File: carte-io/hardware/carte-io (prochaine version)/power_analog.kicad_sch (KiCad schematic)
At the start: 38 parts, among them J1 USB_C_Receptacle_USB2.0_14P, J2 JST-XH_S2B-XH-A, J26 JST-PH-B2B, Q1 IRF9388TRPBF, U16 LT1963AxST-3.3, U2 FT231XQ, U3 LT1963AxST-3.3

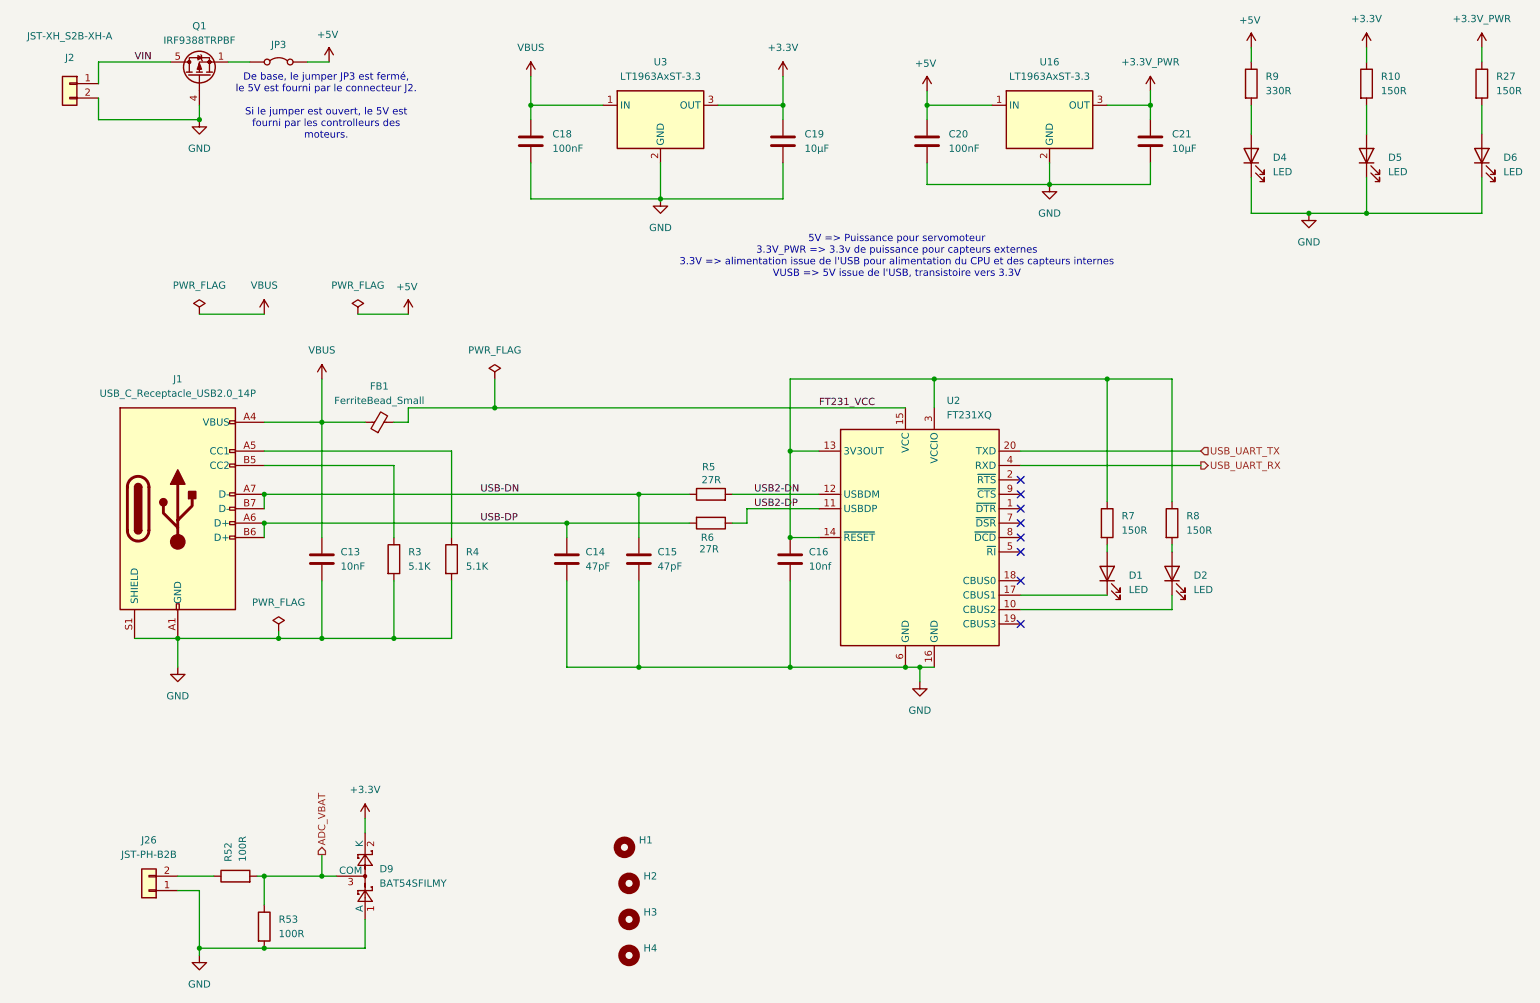
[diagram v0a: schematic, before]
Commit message: Commit de sauvegarde, gros changement sur la carte IO, les connecteurs sont compatibles SeeedStudio Grove. Il faut reprendre une grosse partie du routage et rajouter deux entrées analogiques
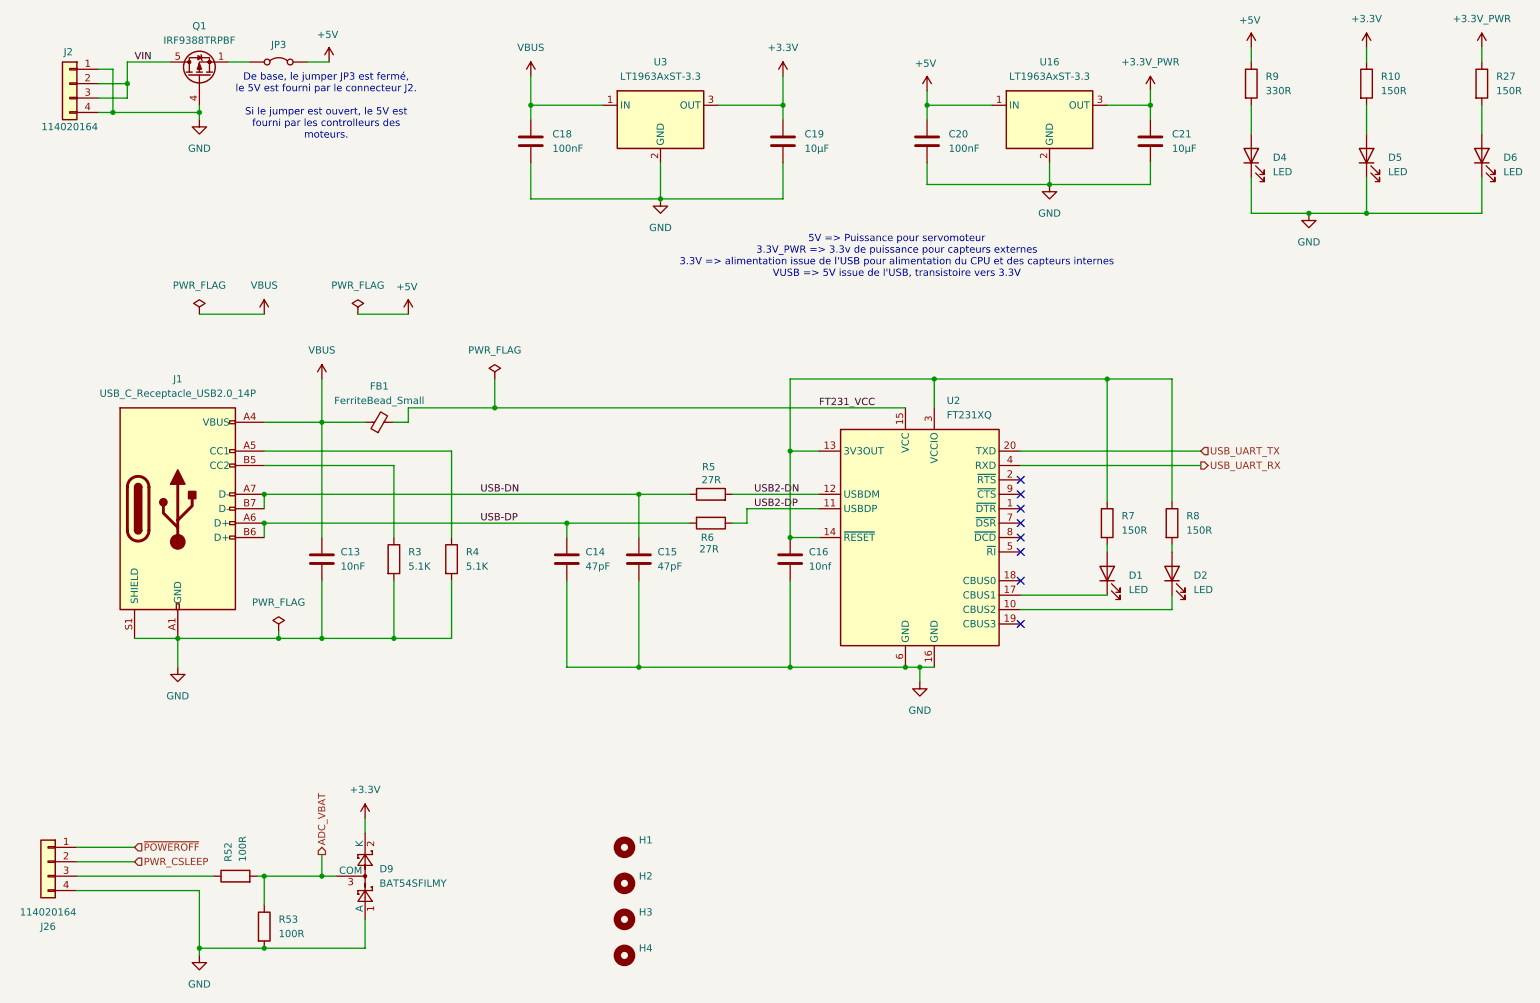
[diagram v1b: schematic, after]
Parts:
- J2: value JST-XH_S2B-XH-A -> 114020164; footprint Connector_JST:JST_XH_S2B-XH-A_1x02_P2.50mm_Horizontal -> SeeedStudio - Horizontal Header -114020164:SEEEDSTUDIO_114020164; symbol Connector_Generic:Conn_01x02 -> SeeedStudio - Horizontal header:SeeedStudio - 114020164 - R/A
- J26: value JST-PH-B2B -> 114020164; footprint Connector_JST:JST_PH_B2B-PH-K_1x02_P2.00mm_Vertical -> SeeedStudio - Horizontal Header -114020164:SEEEDSTUDIO_114020164; symbol Connector_Generic:Conn_01x02 -> SeeedStudio - Horizontal header:SeeedStudio - 114020164 - R/A
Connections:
- net GND: now also J2.1 (Pin_1), J2.4 (Pin_4), J26.4 (Pin_4); no longer J2.2 (Pin_2), J26.1 (Pin_1)
- net VIN: now also J2.2 (Pin_2), J2.3 (Pin_3); no longer J2.1 (Pin_1)
- net at R52.1: now also J26.3 (Pin_3); no longer J26.2 (Pin_2)
- new net PWR_CSLEEP: J26.2 (Pin_2)
- new net ~{POWEROFF}: J26.1 (Pin_1)
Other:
- moved on the sheet: H2, H3, H4
